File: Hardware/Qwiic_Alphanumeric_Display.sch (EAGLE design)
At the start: 15 parts, among them J1 PTH, J2 Qwiic Right Angle, U2 HT16K33

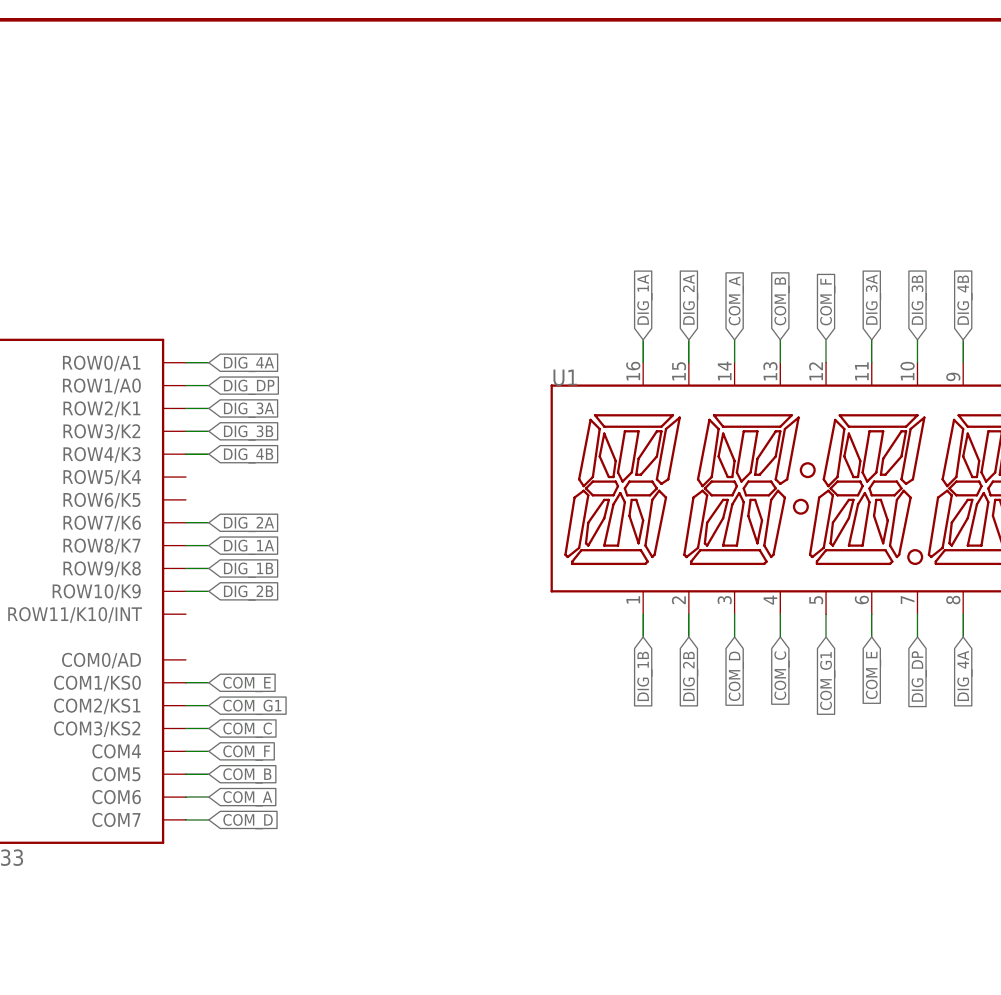
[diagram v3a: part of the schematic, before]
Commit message: New pin assignments
Next: route address jumpers, etc
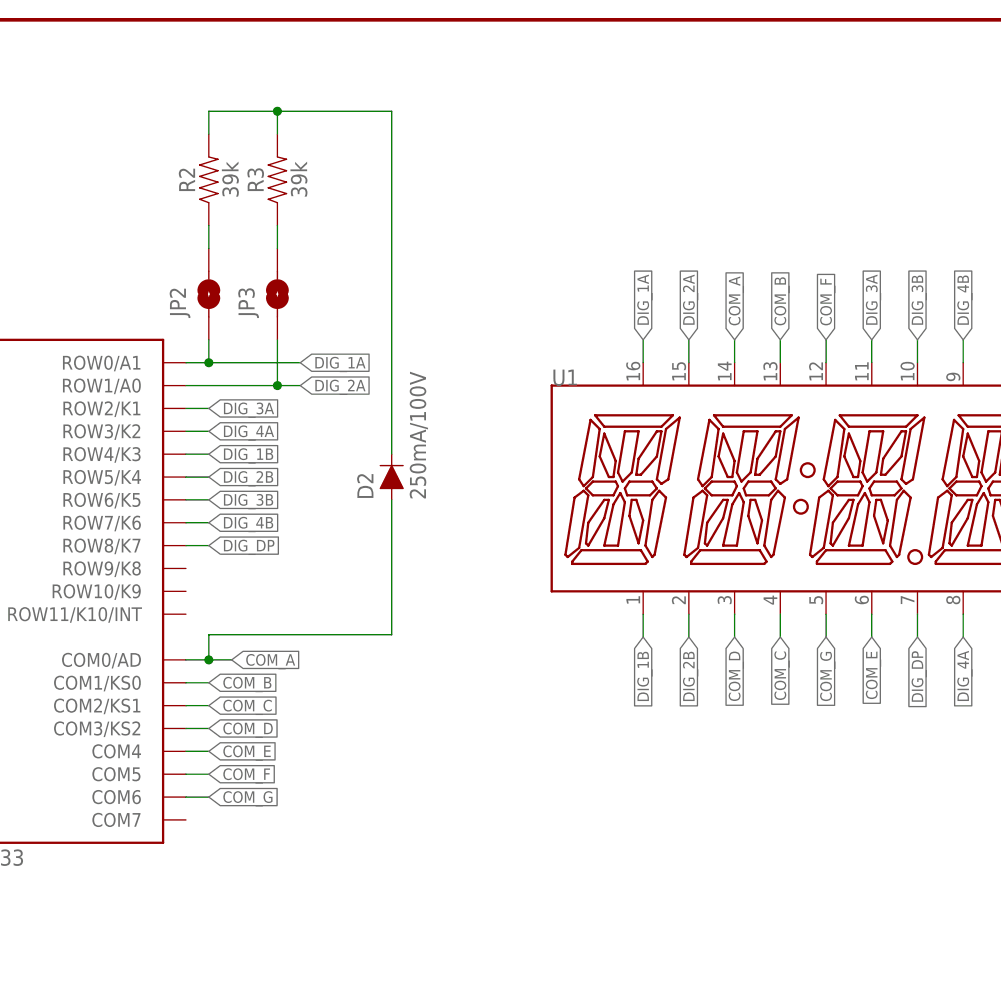
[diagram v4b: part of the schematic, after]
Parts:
- added D2: 250mA/100V, SparkFun-DiscreteSemi:DIODE-BAS16J
- added JP2, JP3: JUMPER-SMT_2_NO_SILK, SparkFun-Jumpers:JUMPER-SMT_2_NO_SILK
- added R2, R3: 39k, SparkFun-Resistors:39KOHM-0603-1/10W-1%
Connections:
- removed net COM_G1: U1.COM_G1, U2.COM2/KS1
- new net COM_G: U1.COM_G1, U2.COM6
- new net N$2: JP2.2, R2.1
- new net N$3: JP3.2, R3.1
- new net N$6: D2.C, R2.2, R3.2
- net COM_A: now also D2.A, U2.COM0/AD; no longer U2.COM6
- net COM_B: now also U2.COM1/KS0; no longer U2.COM5
- net COM_C: now also U2.COM2/KS1; no longer U2.COM3/KS2
- net COM_D: now also U2.COM3/KS2; no longer U2.COM7
- net COM_E: now also U2.COM4; no longer U2.COM1/KS0
- net COM_F: now also U2.COM5; no longer U2.COM4
- net DIG_1A: now also JP2.1, U2.ROW0/A1; no longer U2.ROW8/K7
- net DIG_1B: now also U2.ROW4/K3; no longer U2.ROW9/K8
- net DIG_2A: now also JP3.1, U2.ROW1/A0; no longer U2.ROW7/K6
- net DIG_2B: now also U2.ROW5/K4; no longer U2.ROW10/K9
- net DIG_3B: now also U2.ROW6/K5; no longer U2.ROW3/K2
- net DIG_4A: now also U2.ROW3/K2; no longer U2.ROW0/A1
- net DIG_4B: now also U2.ROW7/K6; no longer U2.ROW4/K3
- net DIG_DP: now also U2.ROW8/K7; no longer U2.ROW1/A0

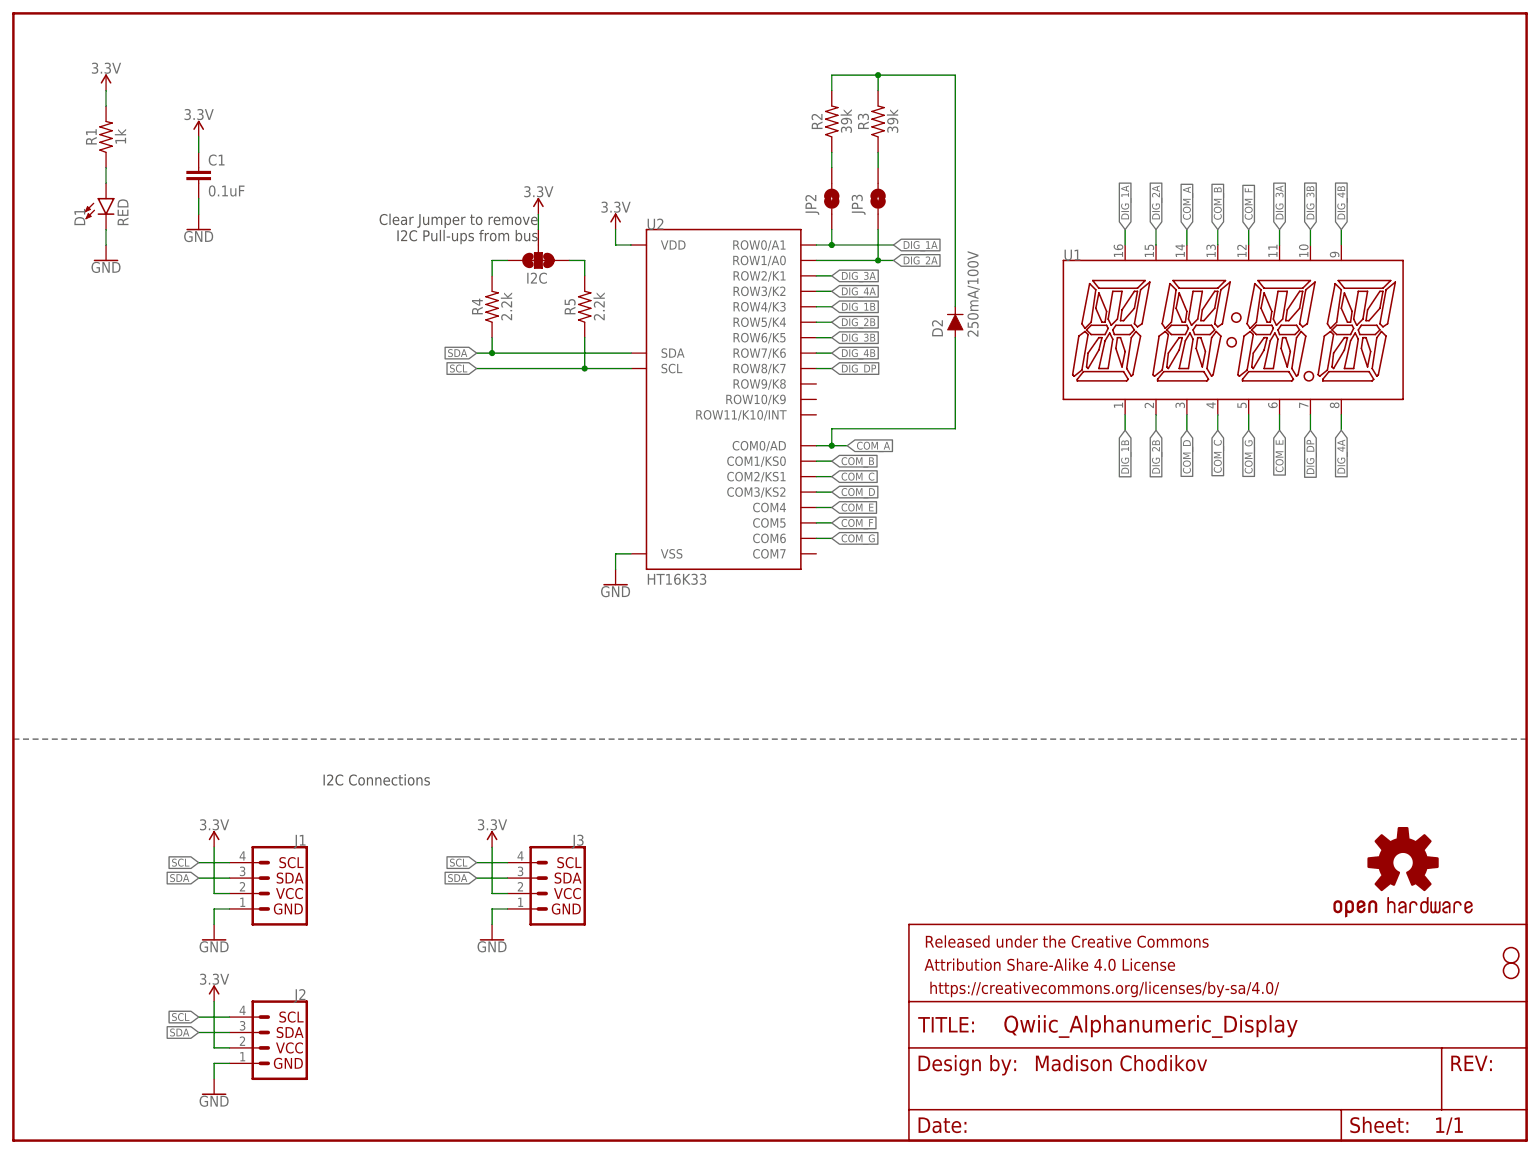
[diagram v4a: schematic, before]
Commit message: Rev X02 of Qwiic Alpha?
Still needs Nate's look-over. Tighter layout, mounting holes, address/power jumpers. Needs V score lines? Where will the silkscreen go?
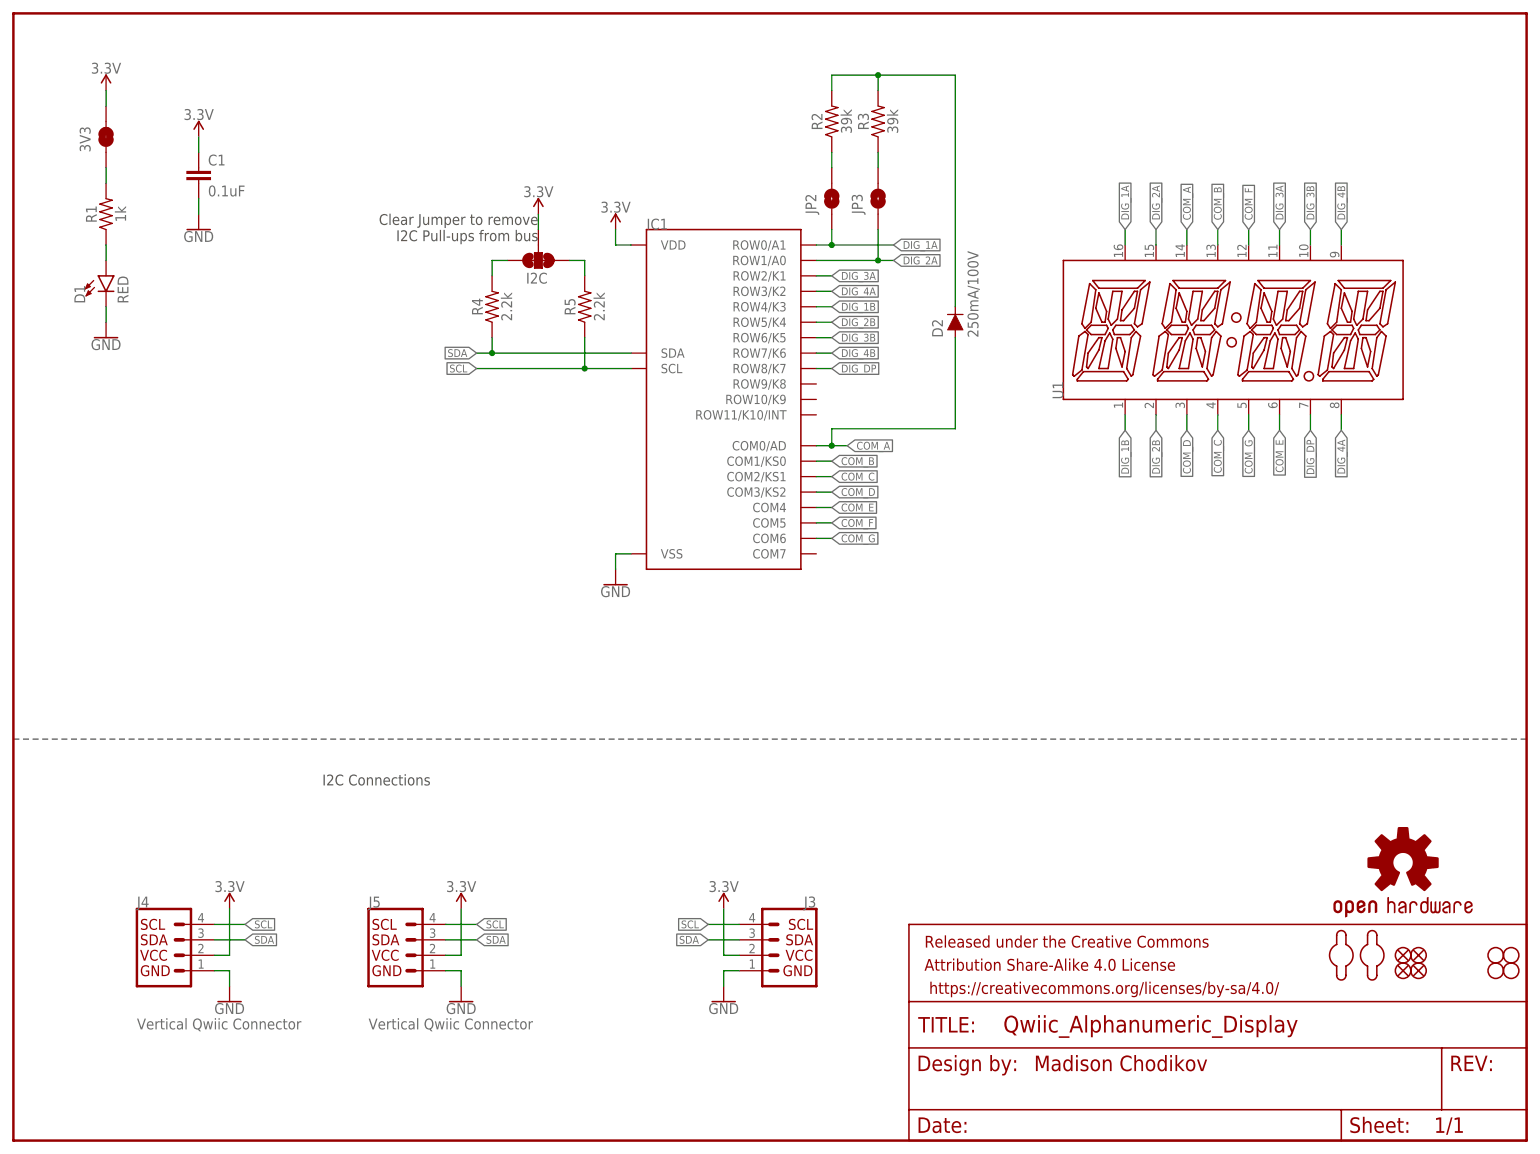
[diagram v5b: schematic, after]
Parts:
- removed J1: PTH, SparkFun-Connectors:I2C_STANDARDQWIIC
- removed J2: Qwiic Right Angle, SparkFun-Connectors:I2C_STANDARDQWIIC
- added 3V3: JUMPER-SMT_2_NC_TRACE_SILK, SparkFun-Jumpers:JUMPER-SMT_2_NC_TRACE_SILK
- added FD1, FD2, FD3, FD4: FIDUCIAL1X2, SparkFun-Aesthetics:FIDUCIAL1X2
- added H1, H2: STAND-OFF, SparkFun-Hardware:STAND-OFF
- added J4, J5: Vertical Qwiic Connector, SparkFun-Connectors:QWIIC_CONNECTOR
- added U$18, U$19: MOUNTING_HOLE_M2-0.4X6, Alphanumeric_Display_Library:MOUNTING_HOLE_M2-0.4X6
- IC1: value HT16K33 -> (none)
- renumbered U2 to IC1
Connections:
- new net N$7: 3V3.1, R1.2
- net 3.3V: now also 3V3.2, J4.2, J5.2; no longer J1.2, J2.2, R1.2
- net GND: now also J4.1, J5.1; no longer J1.1, J2.1
- net SCL: now also J4.4, J5.4; no longer J1.4, J2.4
- net SDA: now also J4.3, J5.3; no longer J1.3, J2.3
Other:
- moved on the sheet: D1, J3, R1

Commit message: Rev X02 ordered!
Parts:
- removed JP1, JP8: STAND-OFF, SparkFun:STAND-OFF
- added H3, H4: STAND-OFF, SparkFun-Hardware:STAND-OFF
- added U$7, U$8: SPARKX-LOGO4, SparkX:SPARKX-LOGO4
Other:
- note added: "0 0 0x70"
- note added: "0 1 0x71"
- note added: "1 0 0x72"
- note added: "1 1 0x73"
- note added: "A1 A0 Address"
- note added: "Default address: 0x70 When no jumpers are closed Floating pin (A0/A1) = 0 Connected to AD = 1"
- moved on the sheet: U1

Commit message: Added missing product ID's
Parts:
- IC1: PROD_ID (none) -> IC-14891
- U1: PROD_ID (none) -> COMP-14892
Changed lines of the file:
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@@
 <grid distance="0.1" unitdist="inch" unit="inch" style="lines" multiple="1" display="no" altdistance="0.01" altunitdist="inch" altunit="inch"/>
 <layers>
-<layer number="1" name="Top" color="4" fill="1" visible="yes" active="no"/>
-<layer number="2" name="Route2" color="16" fill="1" visible="yes" active="no"/>
-<layer number="15" name="Route15" color="23" fill="1" visible="yes" active="no"/>
-<layer number="16" name="Bottom" color="1" fill="1" visible="yes" active="no"/>
-<layer number="17" name="Pads" color="2" fill="1" visible="yes" active="no"/>
-<layer number="18" name="Vias" color="2" fill="1" visible="yes" active="no"/>
-<layer number="19" name="Unrouted" color="6" fill="1" visible="yes" active="no"/>
-<layer number="20" name="Dimension" color="24" fill="1" visible="yes" active="no"/>
-<layer number="21" name="tPlace" color="16" fill="1" visible="yes" active="no"/>
-<layer number="22" name="bPlace" color="14" fill="1" visible="yes" active="no"/>
-<layer number="23" name="tOrigins" color="15" fill="1" visible="yes" active="no"/>
-<layer number="24" name="bOrigins" color="15" fill="1" visible="yes" active="no"/>
-<layer number="25" name="tNames" color="7" fill="1" visible="yes" active="no"/>
-<layer number="26" name="bNames" color="7" fill="1" visible="yes" active="no"/>
-<layer number="27" name="tValues" color="7" fill="1" visible="yes" active="no"/>
-<layer number="28" name="bValues" color="7" fill="1" visible="yes" active="no"/>
+<layer number="1" name="Top" color="4" fill="1" visible="no" active="no"/>
+<layer number="2" name="Route2" color="16" fill="1" visible="no" active="no"/>
+<layer number="15" name="Route15" color="23" fill="1" visible="no" active="no"/>
+<layer number="16" name="Bottom" color="1" fill="1" visible="no" active="no"/>
+<layer number="17" name="Pads" color="2" fill="1" visible="no" active="no"/>
+<layer number="18" name="Vias" color="2" fill="1" visible="no" active="no"/>
+<layer number="19" name="Unrouted" color="6" fill="1" visible="no" active="no"/>
+<layer number="20" name="Dimension" color="24" fill="1" visible="no" active="no"/>
+<layer number="21" name="tPlace" color="16" fill="1" visible="no" active="no"/>
+<layer number="22" name="bPlace" color="14" fill="1" visible="no" active="no"/>
+<layer number="23" name="tOrigins" color="15" fill="1" visible="no" active="no"/>
+<layer number="24" name="bOrigins" color="15" fill="1" visible="no" active="no"/>
+<layer number="25" name="tNames" color="7" fill="1" visible="no" active="no"/>
+<layer number="26" name="bNames" color="7" fill="1" visible="no" active="no"/>
+<layer number="27" name="tValues" color="7" fill="1" visible="no" active="no"/>
+<layer number="28" name="bValues" color="7" fill="1" visible="no" active="no"/>
 <layer number="29" name="tStop" color="7" fill="3" visible="no" active="no"/>
 <layer number="30" name="bStop" color="7" fill="6" visible="no" active="no"/>
@@
 <layer number="35" name="tGlue" color="7" fill="4" visible="no" active="no"/>
 <layer number="36" name="bGlue" color="7" fill="5" visible="no" active="no"/>
-<layer number="37" name="tTest" color="7" fill="1" visible="yes" active="no"/>
-<layer number="38" name="bTest" color="7" fill="1" visible="yes" active="no"/>
+<layer number="37" name="tTest" color="7" fill="1" visible="no" active="no"/>
+<layer number="38" name="bTest" color="7" fill="1" visible="no" active="no"/>
 <layer number="39" name="tKeepout" color="4" fill="11" visible="no" active="no"/>
 <layer number="40" name="bKeepout" color="1" fill="11" visible="no" active="no"/>
@@
 <layer number="44" name="Drills" color="7" fill="1" visible="no" active="no"/>
 <layer number="45" name="Holes" color="7" fill="1" visible="no" active="no"/>
-<layer number="46" name="Milling" color="3" fill="1" visible="yes" active="no"/>
-<layer number="47" name="Measures" color="7" fill="1" visible="yes" active="no"/>
-<layer number="48" name="Document" color="7" fill="1" visible="yes" active="no"/>
-<layer number="49" name="Reference" color="7" fill="1" visible="yes" active="no"/>
-<layer number="50" name="dxf" color="7" fill="1" visible="yes" active="no"/>
-<layer number="51" name="tDocu" color="6" fill="1" visible="yes" active="no"/>
-<layer number="52" name="bDocu" color="7" fill="1" visible="yes" active="no"/>
-<layer number="53" name="tGND_GNDA" color="7" fill="9" visible="yes" active="no"/>
-<layer number="54" name="bGND_GNDA" color="1" fill="9" visible="yes" active="no"/>
-<layer number="56" name="wert" color="7" fill="1" visible="yes" active="no"/>
-<layer number="57" name="tCAD" color="7" fill="1" visible="yes" active="no"/>
-<layer number="59" name="tCarbon" color="7" fill="1" visible="yes" active="no"/>
-<layer number="60" name="bCarbon" color="7" fill="1" visible="yes" active="no"/>
+<layer number="46" name="Milling" color="3" fill="1" visible="no" active="no"/>
+<layer number="47" name="Measures" color="7" fill="1" visible="no" active="no"/>
+<layer number="48" name="Document" color="7" fill="1" visible="no" active="no"/>
+<layer number="49" name="Reference" color="7" fill="1" visible="no" active="no"/>
+<layer number="50" name="dxf" color="7" fill="1" visible="no" active="no"/>
+<layer number="51" name="tDocu" color="6" fill="1" visible="no" active="no"/>
+<layer number="52" name="bDocu" color="7" fill="1" visible="no" active="no"/>
+<layer number="53" name="tGND_GNDA" color="7" fill="9" visible="no" active="no"/>
+<layer number="54" name="bGND_GNDA" color="1" fill="9" visible="no" active="no"/>
+<layer number="56" name="wert" color="7" fill="1" visible="no" active="no"/>
+<layer number="57" name="tCAD" color="7" fill="1" visible="no" active="no"/>
+<layer number="59" name="tCarbon" color="7" fill="1" visible="no" active="no"/>
+<layer number="60" name="bCarbon" color="7" fill="1" visible="no" active="no"/>
 <layer number="88" name="SimResults" color="9" fill="1" visible="yes" active="yes"/>
 <layer number="89" name="SimProbes" color="9" fill="1" visible="yes" active="yes"/>
@@
 <part name="FD3" library="SparkFun-Aesthetics" deviceset="FIDUCIAL" device="1X2"/>
 <part name="FD4" library="SparkFun-Aesthetics" deviceset="FIDUCIAL" device="1X2"/>
-<part name="U1" library="Alphanumeric_Display_Library" deviceset="SILSMART_DISPLAY" device=""/>
+<part name="U1" library="Alphanumeric_Display_Library" deviceset="SILSMART_DISPLAY" device="">
+<attribute name="PROD_ID" value="COMP-14892"/>
+</part>
 <part name="H1" library="SparkFun-Hardware" deviceset="STAND-OFF" device=""/>
 <part name="H2" library="SparkFun-Hardware" deviceset="STAND-OFF" device=""/>
-<part name="IC1" library="Alphanumeric_Display_Library" deviceset="HT16K33" device=""/>
+<part name="IC1" library="Alphanumeric_Display_Library" deviceset="HT16K33" device="">
+<attribute name="PROD_ID" value="IC-14891"/>
+</part>
 <part name="U$18" library="Alphanumeric_Display_Library" deviceset="MOUNTING_HOLE_M2-0.4X6" device=""/>
 <part name="U$19" library="Alphanumeric_Display_Library" deviceset="MOUNTING_HOLE_M2-0.4X6" device=""/>
@@
 <attribute name="NAME" x="177.8" y="86.36" size="1.778" layer="95" rot="R90"/>
 <attribute name="VALUE" x="236.22" y="86.36" size="1.778" layer="96" rot="R90"/>
+<attribute name="PROD_ID" x="205.74" y="99.06" size="1.27" layer="96" display="off"/>
 </instance>
 <instance part="H1" gate="G$1" x="243.84" y="30.48" smashed="yes"/>
@@
 <attribute name="NAME" x="104.14" y="149.86" size="1.778" layer="95"/>
 <attribute name="VALUE" x="104.14" y="91.44" size="1.778" layer="96"/>
+<attribute name="PROD_ID" x="116.84" y="121.92" size="1.27" layer="96" display="off"/>
 </instance>
 <instance part="U$18" gate="G$1" x="223.52" y="30.48" smashed="yes"/>

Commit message: ?
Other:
- note added: "X02"
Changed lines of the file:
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@@
 <wire x1="192.532" y1="160.02" x2="192.532" y2="135.636" width="0.2032" layer="97"/>
 <wire x1="199.898" y1="160.02" x2="199.898" y2="135.89" width="0.2032" layer="97"/>
+<text x="238.76" y="7.62" size="2.54" layer="94">X02</text>
 </plain>
 <instances>
